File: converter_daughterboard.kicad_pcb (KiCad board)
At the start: 2 copper layers, 109.2 x 60.2 mm, 22 parts, among them P1 IN+, P2 IN GND, P3 OUT+, P4 OUT GND, P5 PC, P6 PR, P7 SC, U1 V28C, U2 DAUGHTERBOARD_MOUNT

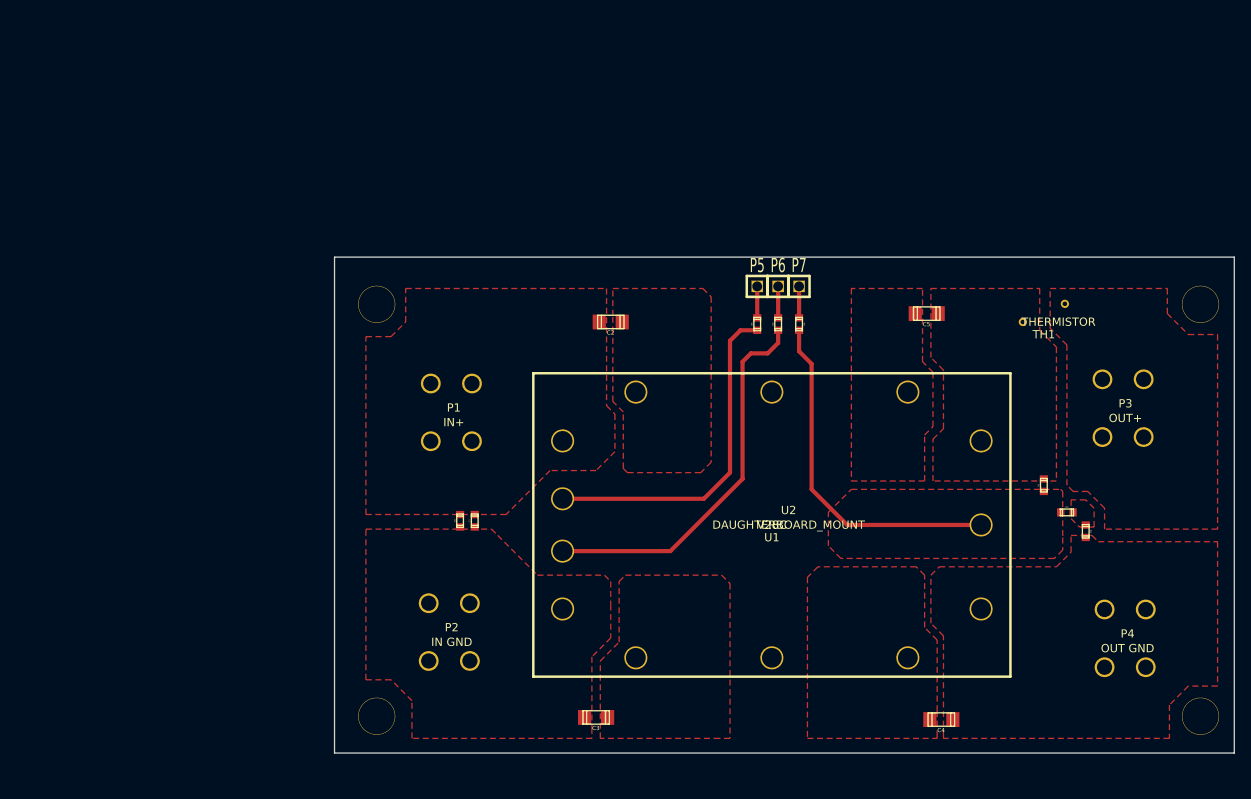
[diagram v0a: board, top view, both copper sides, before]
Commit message: updating converter daughterboard for compatibility with DAC trimming for use with DCMG
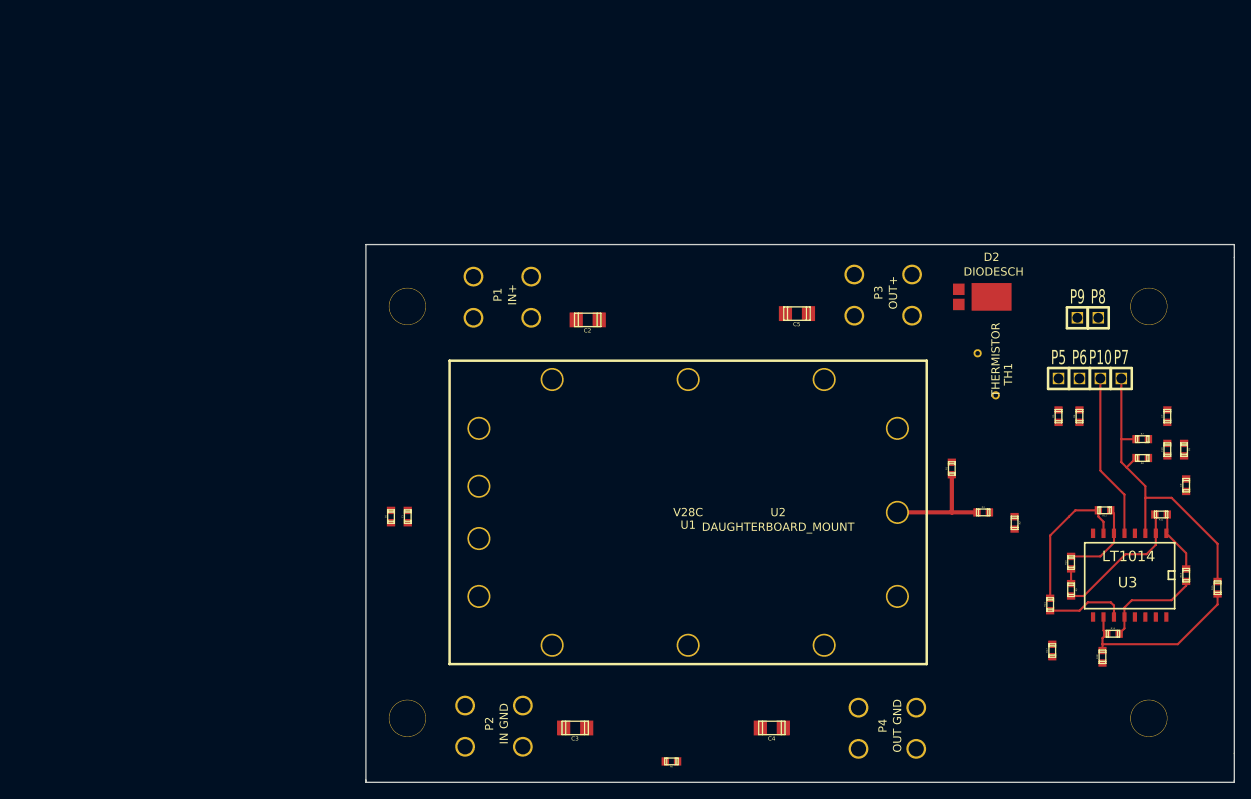
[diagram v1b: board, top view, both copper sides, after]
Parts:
- added C10: .1u, c_0603, F.Cu at (247.7, 133.6)
- added C7: .1u, c_0603, F.Cu at (247.7, 129.5)
- added C8: .1u, c_0603, F.Cu at (249.7, 133.6)
- added C9: .1u, c_0603, F.Cu at (249.9, 137.9)
- added D2: DIODESCH, POWERDI5, F.Cu at (226.3, 115.1)
- added P10: SC-, MOLEX-1, F.Cu at (239.5, 125.0)
- added P8: IC_POW-, MOLEX-1, F.Cu at (239.3, 117.6)
- added P9: IC_POW+, MOLEX-1, F.Cu at (236.7, 117.6)
- added R10: R, c_0603, F.Cu at (236.0, 147.3)
- added R11: R, c_0603, F.Cu at (246.9, 141.5)
- added R12: R, c_0603, F.Cu at (240.0, 141.0)
- added R13: R, c_0603, F.Cu at (249.9, 148.8)
- added R14: R, c_0603, F.Cu at (233.4, 152.4)
- added R15: OPT, c_0603, F.Cu at (253.7, 150.4)
- added R16: R, c_0603, F.Cu at (241.0, 156.0)
- added R17: R, c_0603, F.Cu at (233.7, 158.0)
- added R18: R, c_0603, F.Cu at (239.8, 158.8)
- added R7: R, c_0603, F.Cu at (244.6, 132.3)
- added R8: R, c_0603, F.Cu at (244.6, 134.6)
- added R9: R, c_0603, F.Cu at (236.0, 150.6)
- added U3: LT1014, SO16W, F.Cu at (243.1, 148.8)
- P7: value SC -> SC+
- moved R6 55.3 mm to (187.5, 171.4), turned to 180 degrees
- moved P7 40.7 mm to (242.1, 125.0)
- moved P5 38.2 mm to (234.4, 125.0)
- moved P6 38.2 mm to (237.0, 125.0)
- moved R4 38.2 mm to (237.0, 129.5)
- moved R5 38.2 mm to (234.4, 129.5)
- moved P3 27.4 mm to (216.7, 117.3), turned to 90 degrees
- moved P4 24.9 mm to (217.2, 169.9), turned to 90 degrees
- moved C4 20.6 mm to (199.6, 167.4)
- moved P1 19.3 mm to (170.4, 117.6), turned to 90 degrees
- moved C5 15.7 mm to (202.7, 117.1)
- moved P2 15.5 mm to (169.4, 169.7), turned to 90 degrees
- moved R1 11.4 mm to (221.5, 135.9)
- moved U1 10.3 mm to (189.5, 141.2)
- moved R3 10.2 mm to (225.3, 141.2)
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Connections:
- C1 pad 2: N-0000016 -> GNDA
- C3 pad 1: N-0000016 -> GNDA
- C4 pad 2: N-0000017 (its old number) -> GND
- P2 pad 1: N-0000016 -> GNDA
- P3 pad 1: N-000001 -> N-0000022
- P4 pad 1: N-0000017 (its old number) -> GND
- R1 pad 2: N-000003 -> N-0000018
- R2 pad 1: N-0000017 (its old number) -> GND
- R3 pad 2: N-000003 -> N-0000018
- R6 pad 1: N-000003 -> GNDA
- R6 pad 2: N-0000010 -> GND
- TH1 pad 2: N-000001 -> N-0000027
- U1 pad 4: N-0000016 -> GNDA
- U1 pad 5: N-0000017 (its old number) -> GND
- U1 pad 6: N-000003 -> N-0000018
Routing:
- net N-0000031: track 46.5 -> 0.00 mm
- net N-0000029: track 41.5 -> 0.00 mm
- net N-000003: track 42.3 -> 1.80 mm
- net N-0000010: track 3.82 -> 39.1 mm
- net N-0000025: track 0.00 -> 21.7 mm
- net N-0000011: track 0.00 -> 20.0 mm
- net N-000001: track 0.00 -> 17.8 mm
- net N-000008: track 0.00 -> 16.6 mm
- net N-0000018: track 0.00 -> 14.2 mm
- net N-000002: track 0.00 -> 12.6 mm
- net N-000004: track 0.00 -> 9.99 mm
- net N-000005: track 0.00 -> 9.72 mm
- net N-000007: track 0.00 -> 7.66 mm
- net N-0000030: track 3.82 -> 0.00 mm
- net N-0000028: track 3.82 -> 0.00 mm
- removed copper zone on F.Cu, net N-000001
- removed copper zone on F.Cu, net N-0000013
- removed copper zone on F.Cu, net N-0000014
- removed copper zone on F.Cu, net N-0000016
- removed copper zone on F.Cu, net N-0000017
- removed copper zone on F.Cu, net N-0000017 (its old number)
- removed copper zone on F.Cu, net N-0000020
- removed copper zone on F.Cu, net N-0000026
- removed copper zone on F.Cu, net N-0000028
- removed copper zone on F.Cu, net N-0000029
- removed copper zone on F.Cu, net N-000003
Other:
- board size 109.2 x 60.2 mm -> 105.4 x 65.3 mm

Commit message: added protection circuitry to converter daughterboard. should be ready for fabrication
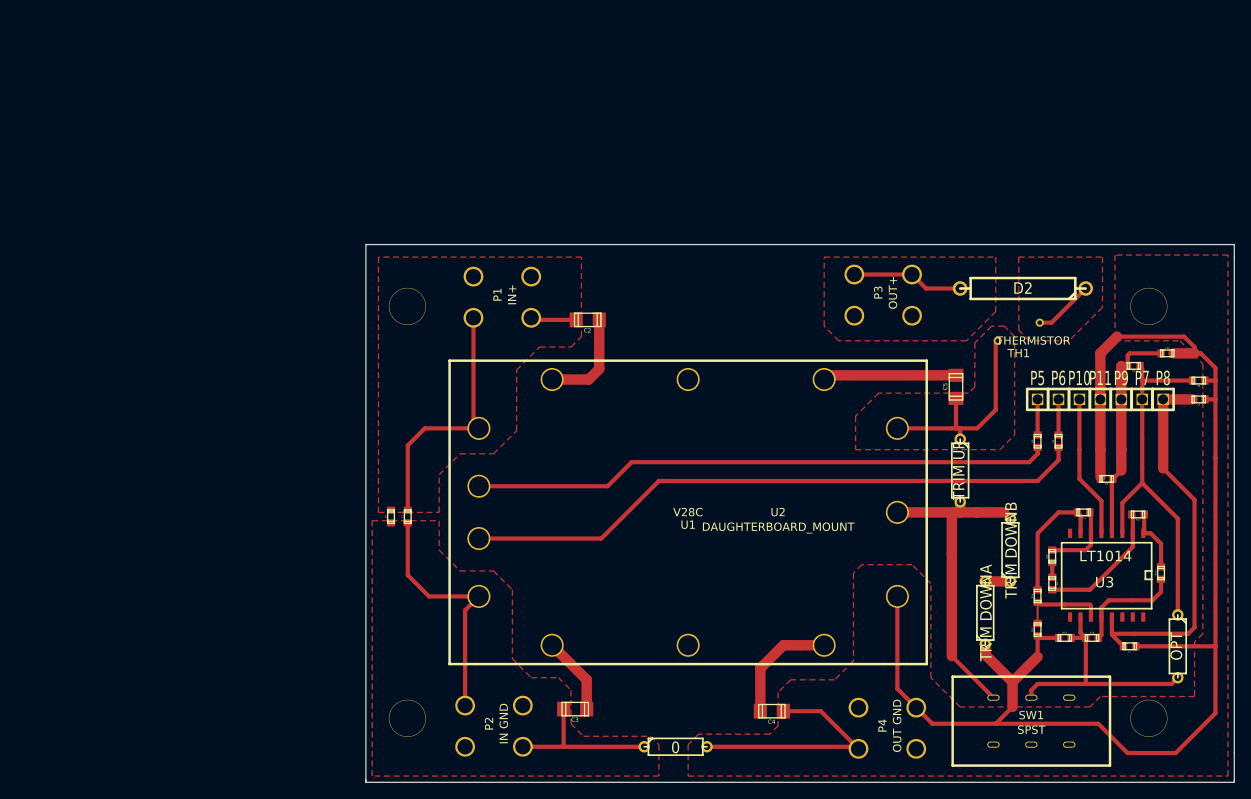
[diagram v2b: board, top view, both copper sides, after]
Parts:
- added P11: gnd, MOLEX-1, F.Cu at (239.5, 127.5)
- added SW1: SPST, L101011MS02_SPDT, F.Cu at (231.1, 169.4)
- D2: footprint POWERDI5 -> R6
- R1: value R -> TRIM UP; footprint c_0603 -> R3
- R15, R6: footprint c_0603 -> R3
- R2: value R -> TRIM DOWNA; footprint c_0603 -> R3
- R3: value R -> TRIM DOWNB; footprint c_0603 -> R3
- R7: value R -> BIAS A
- R8: value R -> BIAS B
- moved C7 28.3 mm to (243.1, 157.5), turned to 180 degrees
- moved C5 21.3 mm to (222.0, 126.0), turned to 90 degrees
- moved P8 12.7 mm to (247.1, 127.5)
- moved C10 11.7 mm to (247.7, 121.9), turned to 0 degrees
- moved R8 11.6 mm to (251.5, 125.2)
- moved R2 11.5 mm to (225.6, 153.4), turned to 90 degrees
- moved P9 11.3 mm to (242.1, 127.5)
- moved C9 9.68 mm to (240.3, 137.2), turned to 180 degrees
- moved R7 8.95 mm to (243.6, 123.4), turned to 180 degrees
- moved R15 8.59 mm to (248.9, 157.5), turned to 270 degrees
- moved C8 6.35 mm to (251.5, 127.5), turned to 180 degrees
- moved R3 5.64 mm to (228.6, 145.8), turned to 90 degrees
- moved R18 5.11 mm to (235.2, 156.5), turned to 0 degrees
- moved TH1 4.93 mm to (229.6, 120.4), turned to 0 degrees
- moved R5 3.97 mm to (231.9, 132.6)
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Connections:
- U3 pad 13: (no net) -> IC_POW-
- U3 pad 4: (no net) -> IC_POW+
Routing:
- net GND: track 0.00 -> 194.7 mm
- net N-0000029: track 0.00 -> 75.8 mm
- net N-0000027: track 0.00 -> 70.2 mm
- net GNDA: track 0.00 -> 49.4 mm
- net IC_POW-: track 0.00 -> 47.3 mm
- net N-0000030: track 0.00 -> 36.6 mm
- net IC_POW+: track 0.00 -> 27.0 mm
- net N-0000020: track 0.00 -> 26.3 mm
- net N-0000017: track 14.2 -> 39.9 mm
- net N-0000013: track 0.00 -> 16.2 mm
- net N-0000014: track 0.00 -> 14.1 mm
- net N-0000021: track 0.00 -> 13.6 mm
- net N-0000019: track 0.00 -> 12.2 mm
- net N-0000018: track 0.00 -> 9.48 mm
- net N-0000022: track 21.7 -> 29.5 mm
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- added copper zone on F.Cu, net GND
- added copper zone on F.Cu, net GNDA
- added copper zone on F.Cu, net N-0000020
- added copper zone on F.Cu, net N-0000021
- added copper zone on F.Cu, net N-0000025
- added copper zone on F.Cu, net N-0000030

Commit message: added silkscreen labels
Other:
- board text added: "AMP BYPASS"
- board text added: "DAC TRIM ON/OFF"
- board text added: "IC POW-"
- board text added: "IN +"
- board text added: "IN -"
- board text added: "OUT +"
- board text added: "OUT -"
- board text added: "PC"
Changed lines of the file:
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@@
     (area 150.317999 108.661999 255.828001 174.040001)
     (thickness 1.6)
-    (drawings 8)
+    (drawings 16)
     (tracks 190)
     (zones 0)
@@
     )
   )
+  (gr_text "DAC TRIM\nON/OFF" (at 249.174 169.926) (layer F.SilkS)
+    (effects (font (size 1.5 1.5) (thickness 0.3)))
+  )
+  (gr_text "AMP BYPASS" (at 252.984 157.48 90) (layer F.SilkS)
+    (effects (font (size 1.5 1.5) (thickness 0.3)))
+  )
+  (gr_text "IC POW-" (at 249.682 131.064) (layer F.SilkS)
+    (effects (font (size 1.5 1.5) (thickness 0.3)))
+  )
+  (gr_text PC (at 231.394 122.682) (layer F.SilkS)
+    (effects (font (size 1.5 1.5) (thickness 0.3)))
+  )
+  (gr_text "OUT -" (at 202.692 170.18) (layer F.SilkS)
+    (effects (font (size 3 2) (thickness 0.3)))
+  )
+  (gr_text "OUT +" (at 201.168 113.538) (layer F.SilkS)
+    (effects (font (size 3 2) (thickness 0.3)))
+  )
+  (gr_text "IN -" (at 176.022 170.434) (layer F.SilkS)
+    (effects (font (size 3 2) (thickness 0.3)))
+  )
+  (gr_text "IN +" (at 178.562 113.538) (layer F.SilkS)
+    (effects (font (size 3 2) (thickness 0.3)))
+  )
   (gr_line (start 255.778 173.99) (end 255.778 173.736) (angle 90) (layer Edge.Cuts) (width 0.1))

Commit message: updated converter board and created fab files
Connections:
- C6 pad 2: (no net) -> GNDA
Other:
- board text added: "DC/DC DAUGHTERBOARD Rev B March 25, 2016"

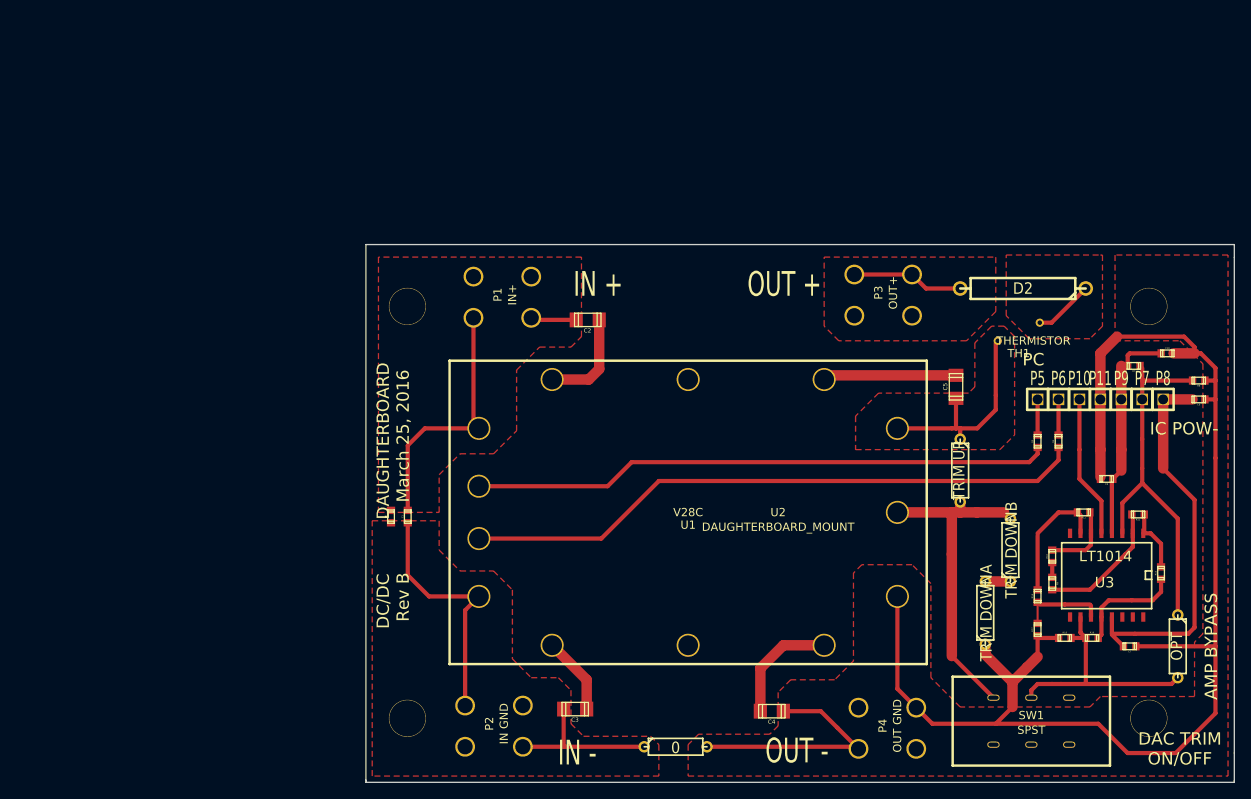
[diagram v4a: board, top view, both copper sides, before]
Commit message: revised converter daughterboard to adjust setpoint signal to account for current dropped across low side sense resistor
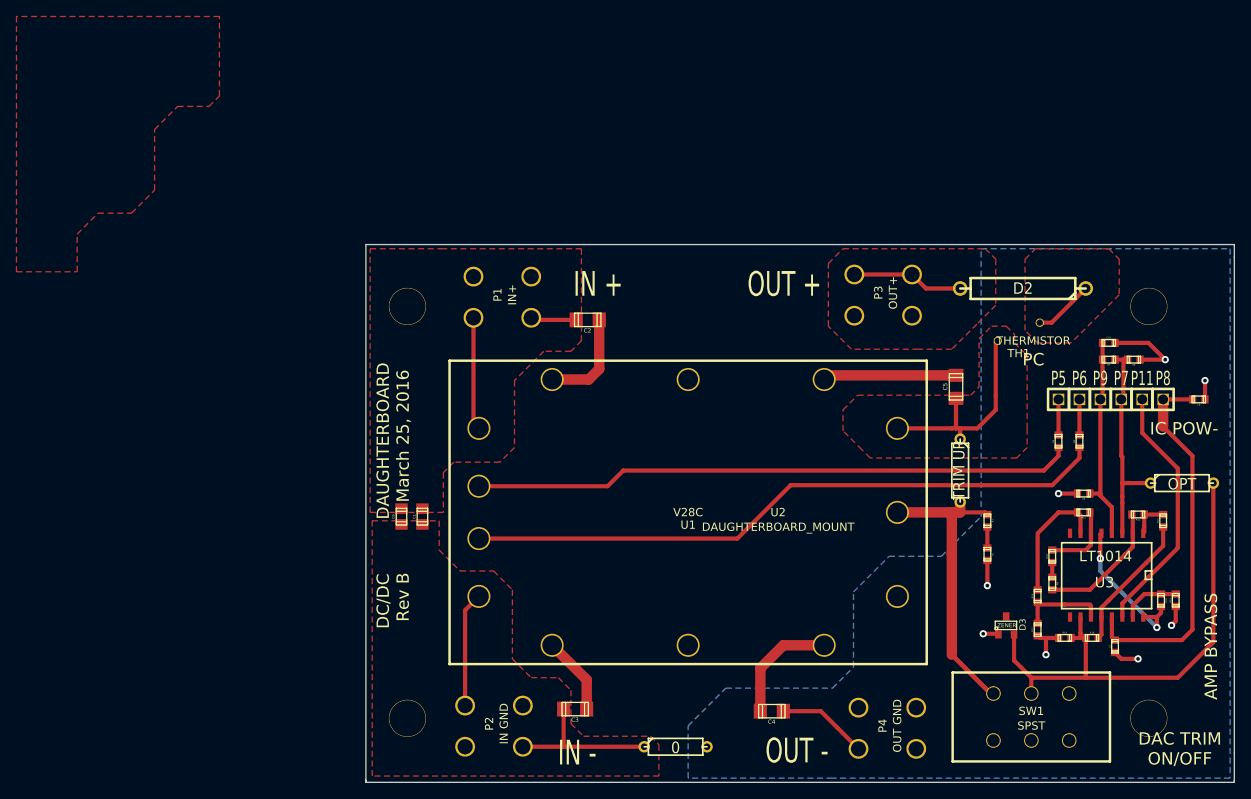
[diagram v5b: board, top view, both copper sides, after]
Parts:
- removed P10: SC-, MOLEX-1
- added D3: ZENER, SOT23, F.Cu at (228.1, 154.9)
- added R19: R, c_0603, F.Cu at (248.7, 151.9)
- added R20: R, c_0603, F.Cu at (246.9, 151.9)
- C1, C6: footprint c_0603 -> c_0805
- P11: value gnd -> SC-
- R2, R3: footprint R3 -> c_0603
- moved R15 19.8 mm to (249.4, 137.7), turned to 0 degrees
- moved R8 8.27 mm to (243.6, 122.7)
- moved C10 7.22 mm to (240.5, 120.7)
- moved R2 7.12 mm to (225.8, 146.3), turned to 270 degrees
- moved R13 6.36 mm to (247.1, 142.2)
- moved P11 5.08 mm to (244.6, 127.5)
- moved R3 4.52 mm to (225.8, 142.2), turned to 270 degrees
- moved C9 3.31 mm to (237.5, 138.9)
- moved R7 3.14 mm to (240.5, 122.7)
- moved P5 2.54 mm to (234.4, 127.5)
- moved P9 2.54 mm to (239.5, 127.5)
- moved R5 2.54 mm to (234.4, 132.6)
- moved P6 2.54 mm to (237.0, 127.5)
- moved P7 2.54 mm to (242.1, 127.5)
- moved R4 2.54 mm to (237.0, 132.6)
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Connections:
- P11 pad 1: GND -> N-0000011
- U3 pad 14: (no net) -> N-0000011
- U3 pad 15: (no net) -> N-0000010
- U3 pad 16: (no net) -> N-0000015
- U3 pad 5: N-0000011 -> N-0000015
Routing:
- net GND: track 194.7 -> 41.2 mm, vias 0 -> 8
- net N-000009: track 29.5 -> 60.5 mm
- net N-0000012: track 45.3 -> 26.2 mm
- net N-0000015: track 0.00 -> 18.7 mm, vias 0 -> 2
- net N-0000032: track 36.6 -> 19.3 mm
- net GNDA: track 49.4 -> 33.4 mm
- net N-0000011: track 17.4 -> 31.0 mm
- net N-0000010: track 0.00 -> 7.19 mm
- net N-0000021: track 39.9 -> 43.2 mm
- net N-000008: track 13.4 -> 16.7 mm
- net N-000003: track 7.82 -> 4.63 mm
- net N-0000027: track 70.2 -> 72.9 mm
- net N-0000026: track 75.8 -> 78.2 mm
- net IC_POW+: track 27.0 -> 25.1 mm
- net IC_POW-: track 47.3 -> 45.9 mm
- added copper zone on B.Cu, net GND
- removed copper zone on F.Cu, net GND
